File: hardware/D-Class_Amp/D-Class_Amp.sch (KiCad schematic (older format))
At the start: 25 parts, among them J101 Barrel_Jack_MountingPin, J102 AudioJack2, U101 NCP1117-12_TO252, U102 MCP1799T-5002H_TT

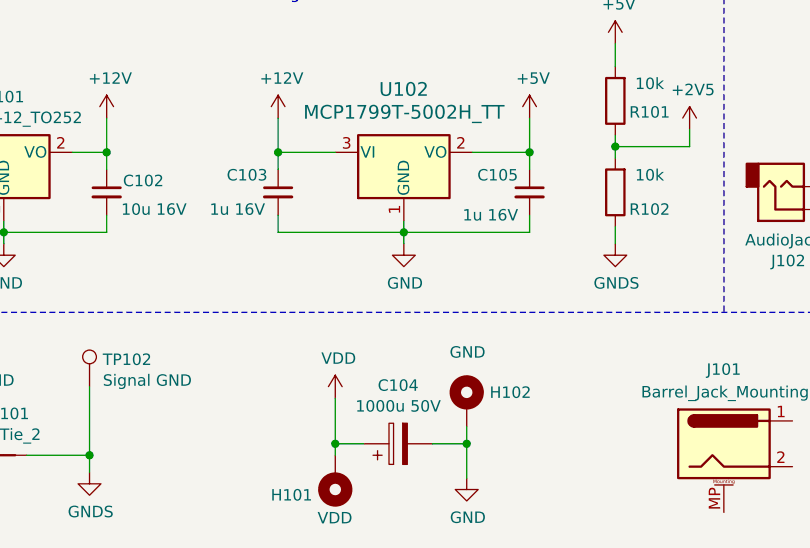
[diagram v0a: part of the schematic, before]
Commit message: Designed the triangle generator PCB layout, and the power switching stage layout
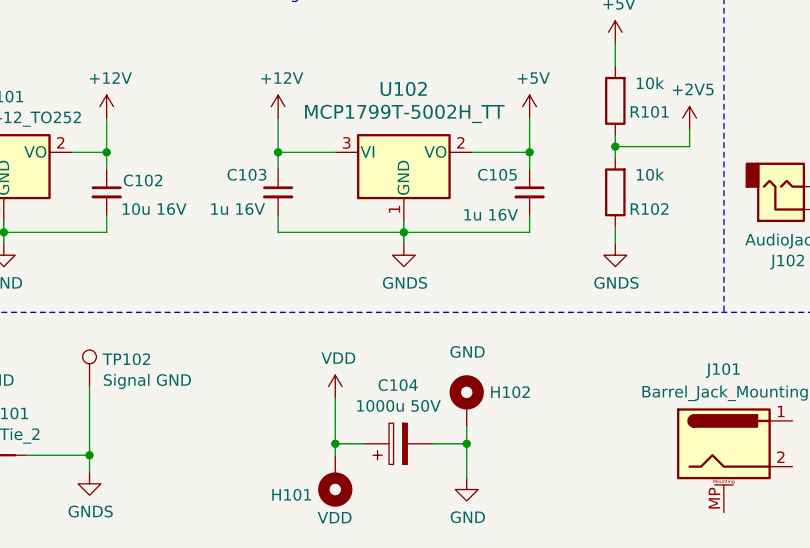
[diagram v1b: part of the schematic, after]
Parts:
- H101, H102: footprint (none) -> MountingHole:MountingHole_3mm_Pad_Via
- NT101: footprint (none) -> NetTie:NetTie-2_SMD_Pad2.0mm
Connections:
- net GND: no longer C103.2, C105.2, U102.1 (GND)
- net GNDS: now also C103.2, C105.2, U102.1 (GND)
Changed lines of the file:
@@
 $EndComp
 $Comp
-L power:GND #PWR0101
+L power:GND #PWR0102
 U 1 1 612A56C1
 P 900 2675
-F 0 "#PWR0101" H 900 2425 50  0001 C CNN
+F 0 "#PWR0102" H 900 2425 50  0001 C CNN
 F 1 "GND" H 905 2502 50  0000 C CNN
 F 2 "" H 900 2675 50  0001 C CNN
@@
 F 0 "NT101" H 1300 2781 50  0000 C CNN
 F 1 "Net-Tie_2" H 1300 2690 50  0000 C CNN
-F 2 "" H 1300 2600 50  0001 C CNN
+F 2 "NetTie:NetTie-2_SMD_Pad2.0mm" H 1300 2600 50  0001 C CNN
 F 3 "~" H 1300 2600 50  0001 C CNN
 	1    1300 2600
@@
 Wire Wire Line
 	1675 2600 1675 2675
-$Comp
-L Connector:TestPoint TP103
-U 1 1 61126C37
-P 5175 800
-F 0 "TP103" H 5233 918 50  0000 L CNN
-F 1 "Audio In" H 5233 827 50  0000 L CNN
-F 2 "TestPoint:TestPoint_THTPad_D2.0mm_Drill1.0mm" H 5375 800 50  0001 C CNN
-F 3 "~" H 5375 800 50  0001 C CNN
-	1    5175 800
-	1    0    0    -1
-$EndComp
-$Comp
-L Connector:TestPoint TP104
-U 1 1 6112780B
-P 6425 800
-F 0 "TP104" H 6483 918 50  0000 L CNN
-F 1 "Input Filter" H 6483 827 50  0000 L CNN
-F 2 "TestPoint:TestPoint_THTPad_D2.0mm_Drill1.0mm" H 6625 800 50  0001 C CNN
-F 3 "~" H 6625 800 50  0001 C CNN
-	1    6425 800
-	1    0    0    -1
-$EndComp
 Wire Wire Line
 	10075 1525 10325 1525
@@
 	1    0    0    -1
 $EndComp
-$Comp
-L Connector:TestPoint TP106
-U 1 1 61129DBB
-P 7775 775
-F 0 "TP106" H 7833 899 50  0000 L CNN
-F 1 "~S-PWM" H 7833 801 50  0000 L CNN
-F 2 "TestPoint:TestPoint_THTPad_D2.0mm_Drill1.0mm" H 7975 775 50  0001 C CNN
-F 3 "~" H 7975 775 50  0001 C CNN
-	1    7775 775
-	1    0    0    -1
-$EndComp
-$Comp
-L Connector:TestPoint TP107
-U 1 1 6112D71A
-P 8825 775
-F 0 "TP107" H 8750 875 50  0000 R CNN
-F 1 "P_Out" H 8550 800 50  0000 L CNN
-F 2 "TestPoint:TestPoint_THTPad_D2.0mm_Drill1.0mm" H 9025 775 50  0001 C CNN
-F 3 "~" H 9025 775 50  0001 C CNN
-	1    8825 775
-	1    0    0    -1
-$EndComp
-$Comp
-L Connector:TestPoint TP108
-U 1 1 6112D764
-P 8975 775
-F 0 "TP108" H 9033 899 50  0000 L CNN
-F 1 "~P_Out" H 9033 801 50  0000 L CNN
-F 2 "TestPoint:TestPoint_THTPad_D2.0mm_Drill1.0mm" H 9175 775 50  0001 C CNN
-F 3 "~" H 9175 775 50  0001 C CNN
-	1    8975 775
-	1    0    0    -1
-$EndComp
 Wire Wire Line
 	8825 775  8825 1325
@@
 Wire Wire Line
 	5175 1425 5375 1425
-$Comp
-L Connector:TestPoint TP110
-U 1 1 6113731F
-P 10325 775
-F 0 "TP110" H 10383 893 50  0000 L CNN
-F 1 "~Speaker_Out" H 10383 802 50  0000 L CNN
-F 2 "TestPoint:TestPoint_THTPad_D2.0mm_Drill1.0mm" H 10525 775 50  0001 C CNN
-F 3 "~" H 10525 775 50  0001 C CNN
-	1    10325 775
-	1    0    0    -1
-$EndComp
 Wire Wire Line
 	10175 775  10175 1325
@@
 Wire Wire Line
 	10325 1525 10425 1525
-$Comp
-L Connector:TestPoint TP105
-U 1 1 6112B1A8
-P 7625 775
-F 0 "TP105" H 7550 875 50  0000 R CNN
-F 1 "S-PWM" H 7300 800 50  0000 L CNN
-F 2 "TestPoint:TestPoint_THTPad_D2.0mm_Drill1.0mm" H 7825 775 50  0001 C CNN
-F 3 "~" H 7825 775 50  0001 C CNN
-	1    7625 775
-	1    0    0    -1
-$EndComp
-$Comp
-L Connector:TestPoint TP109
-U 1 1 611372D5
-P 10175 775
-F 0 "TP109" H 10100 875 50  0000 R CNN
-F 1 "Speaker_Out" H 9700 800 50  0000 L CNN
-F 2 "TestPoint:TestPoint_THTPad_D2.0mm_Drill1.0mm" H 10375 775 50  0001 C CNN
-F 3 "~" H 10375 775 50  0001 C CNN
-	1    10175 775
-	1    0    0    -1
-$EndComp
 Text Notes 850  700  0    50   ~ 0
 12V Reg\n\n
@@
 P 850 1125
 AR Path="/610497A4/611CA11C" Ref="#PWR?"  Part="1"
-AR Path="/611CA11C" Ref="#PWR0102"  Part="1"
-F 0 "#PWR0102" H 850 975 50  0001 C CNN
+AR Path="/611CA11C" Ref="#PWR0101"  Part="1"
+F 0 "#PWR0101" H 850 975 50  0001 C CNN
 F 1 "VDD" H 865 1298 50  0000 C CNN
 F 2 "" H 850 1125 50  0001 C CNN
 F 3 "" H 850 1125 50  0001 C CNN
 	1    850  1125
-	1    0    0    -1
-$EndComp
-$Comp
-L power:GND #PWR?
-U 1 1 611CA122
-P 1300 1675
-AR Path="/610497A4/611CA122" Ref="#PWR?"  Part="1"
-AR Path="/611CA122" Ref="#PWR0103"  Part="1"
-F 0 "#PWR0103" H 1300 1425 50  0001 C CNN
-F 1 "GND" H 1305 1502 50  0000 C CNN
-F 2 "" H 1300 1675 50  0001 C CNN
-F 3 "" H 1300 1675 50  0001 C CNN
-	1    1300 1675
 	1    0    0    -1
 $EndComp
@@
 Text Notes 2350 700  0    50   ~ 0
 5V Reg\n\n
-$Comp
-L power:GND #PWR?
-U 1 1 611FCDB4
-P 3050 1675
-AR Path="/610497A4/611FCDB4" Ref="#PWR?"  Part="1"
-AR Path="/611FCDB4" Ref="#PWR0108"  Part="1"
-F 0 "#PWR0108" H 3050 1425 50  0001 C CNN
-F 1 "GND" H 3055 1502 50  0000 C CNN
-F 2 "" H 3050 1675 50  0001 C CNN
-F 3 "" H 3050 1675 50  0001 C CNN
-	1    3050 1675
-	1    0    0    -1
-$EndComp
 Wire Wire Line
 	3050 1625 3050 1675
 Wire Notes Line
 	450  1975 11225 1975
-$Comp
-L Connector:TestPoint TP101
-U 1 1 6113B2E7
-P 900 2300
-F 0 "TP101" H 958 2418 50  0000 L CNN
-F 1 "Power GND" H 958 2327 50  0000 L CNN
-F 2 "TestPoint:TestPoint_THTPad_D2.0mm_Drill1.0mm" H 1100 2300 50  0001 C CNN
-F 3 "~" H 1100 2300 50  0001 C CNN
-	1    900  2300
-	1    0    0    -1
-$EndComp
-$Comp
-L Connector:TestPoint TP102
-U 1 1 6113B863
-P 1675 2300
-F 0 "TP102" H 1733 2418 50  0000 L CNN
-F 1 "Signal GND" H 1733 2327 50  0000 L CNN
-F 2 "TestPoint:TestPoint_THTPad_D2.0mm_Drill1.0mm" H 1875 2300 50  0001 C CNN
-F 3 "~" H 1875 2300 50  0001 C CNN
-	1    1675 2300
-	1    0    0    -1
-$EndComp
 Wire Wire Line
 	900  2300 900  2600
@@
 F 0 "H102" H 3425 2424 50  0000 L CNN
 F 1 "GND" H 3250 2600 50  0000 L CNN
-F 2 "" H 3325 2375 50  0001 C CNN
+F 2 "MountingHole:MountingHole_3mm_Pad_Via" H 3325 2375 50  0001 C CNN
 F 3 "~" H 3325 2375 50  0001 C CNN
 	1    3325 2375
@@
 F 0 "H101" H 2850 2775 50  0000 L CNN
 F 1 "VDD" H 2675 2875 50  0000 L CNN
-F 2 "" H 2750 2700 50  0001 C CNN
+F 2 "MountingHole:MountingHole_3mm_Pad_Via" H 2750 2700 50  0001 C CNN
 F 3 "~" H 2750 2700 50  0001 C CNN
 	1    2750 2700
@@
 	1    0    0    -1
 $EndComp
+$Comp
+L Connector:TestPoint TP110
+U 1 1 6113731F
+P 10325 775
+F 0 "TP110" H 10383 893 50  0000 L CNN
+F 1 "~Speaker_Out" H 10383 802 50  0000 L CNN
+F 2 "TestPoint:TestPoint_THTPad_D2.0mm_Drill1.0mm" H 10525 775 50  0001 C CNN
+F 3 "~" H 10525 775 50  0001 C CNN
+	1    10325 775
+	1    0    0    -1
+$EndComp
+$Comp
+L Connector:TestPoint TP109
+U 1 1 611372D5
+P 10175 775
+F 0 "TP109" H 10100 875 50  0000 R CNN
+F 1 "Speaker_Out" H 9700 800 50  0000 L CNN
+F 2 "TestPoint:TestPoint_THTPad_D2.0mm_Drill1.0mm" H 10375 775 50  0001 C CNN
+F 3 "~" H 10375 775 50  0001 C CNN
+	1    10175 775
+	1    0    0    -1
+$EndComp
+$Comp
+L Connector:TestPoint TP108
+U 1 1 6112D764
+P 8975 775
+F 0 "TP108" H 9033 899 50  0000 L CNN
+F 1 "~P_Out" H 9033 801 50  0000 L CNN
+F 2 "TestPoint:TestPoint_THTPad_D2.0mm_Drill1.0mm" H 9175 775 50  0001 C CNN
+F 3 "~" H 9175 775 50  0001 C CNN
+	1    8975 775
+	1    0    0    -1
+$EndComp
+$Comp
+L Connector:TestPoint TP107
+U 1 1 6112D71A
+P 8825 775
+F 0 "TP107" H 8750 875 50  0000 R CNN
+F 1 "P_Out" H 8550 800 50  0000 L CNN
+F 2 "TestPoint:TestPoint_THTPad_D2.0mm_Drill1.0mm" H 9025 775 50  0001 C CNN
+F 3 "~" H 9025 775 50  0001 C CNN
+	1    8825 775
+	1    0    0    -1
+$EndComp
+$Comp
+L Connector:TestPoint TP106
+U 1 1 61129DBB
+P 7775 775
+F 0 "TP106" H 7833 899 50  0000 L CNN
+F 1 "~S-PWM" H 7833 801 50  0000 L CNN
+F 2 "TestPoint:TestPoint_THTPad_D2.0mm_Drill1.0mm" H 7975 775 50  0001 C CNN
+F 3 "~" H 7975 775 50  0001 C CNN
+	1    7775 775
+	1    0    0    -1
+$EndComp
+$Comp
+L Connector:TestPoint TP105
+U 1 1 6112B1A8
+P 7625 775
+F 0 "TP105" H 7550 875 50  0000 R CNN
+F 1 "S-PWM" H 7300 800 50  0000 L CNN
+F 2 "TestPoint:TestPoint_THTPad_D2.0mm_Drill1.0mm" H 7825 775 50  0001 C CNN
+F 3 "~" H 7825 775 50  0001 C CNN
+	1    7625 775
+	1    0    0    -1
+$EndComp
+$Comp
+L Connector:TestPoint TP104
+U 1 1 6112780B
+P 6425 800
+F 0 "TP104" H 6483 918 50  0000 L CNN
+F 1 "Input Filter" H 6483 827 50  0000 L CNN
+F 2 "TestPoint:TestPoint_THTPad_D2.0mm_Drill1.0mm" H 6625 800 50  0001 C CNN
+F 3 "~" H 6625 800 50  0001 C CNN
+	1    6425 800
+	1    0    0    -1
+$EndComp
+$Comp
+L Connector:TestPoint TP103
+U 1 1 61126C37
+P 5175 800
+F 0 "TP103" H 5233 918 50  0000 L CNN
+F 1 "Audio In" H 5233 827 50  0000 L CNN
+F 2 "TestPoint:TestPoint_THTPad_D2.0mm_Drill1.0mm" H 5375 800 50  0001 C CNN
+F 3 "~" H 5375 800 50  0001 C CNN
+	1    5175 800
+	1    0    0    -1
+$EndComp
+$Comp
+L Connector:TestPoint TP102
+U 1 1 6113B863
+P 1675 2300
+F 0 "TP102" H 1733 2418 50  0000 L CNN
+F 1 "Signal GND" H 1733 2327 50  0000 L CNN
+F 2 "TestPoint:TestPoint_THTPad_D2.0mm_Drill1.0mm" H 1875 2300 50  0001 C CNN
+F 3 "~" H 1875 2300 50  0001 C CNN
+	1    1675 2300
+	1    0    0    -1
+$EndComp
+$Comp
+L Connector:TestPoint TP101
+U 1 1 6113B2E7
+P 900 2300
+F 0 "TP101" H 958 2418 50  0000 L CNN
+F 1 "Power GND" H 958 2327 50  0000 L CNN
+F 2 "TestPoint:TestPoint_THTPad_D2.0mm_Drill1.0mm" H 1100 2300 50  0001 C CNN
+F 3 "~" H 1100 2300 50  0001 C CNN
+	1    900  2300
+	1    0    0    -1
+$EndComp
+$Comp
+L power:GNDS #PWR0103
+U 1 1 61218DB5
+P 3050 1675
+F 0 "#PWR0103" H 3050 1425 50  0001 C CNN
+F 1 "GNDS" H 3055 1502 50  0000 C CNN
+F 2 "" H 3050 1675 50  0001 C CNN
+F 3 "" H 3050 1675 50  0001 C CNN
+	1    3050 1675
+	1    0    0    -1
+$EndComp
+$Comp
+L power:GND #PWR?
+U 1 1 611FCDB4
+P 1300 1675
+AR Path="/610497A4/611FCDB4" Ref="#PWR?"  Part="1"
+AR Path="/611FCDB4" Ref="#PWR0108"  Part="1"
+F 0 "#PWR0108" H 1300 1425 50  0001 C CNN
+F 1 "GND" H 1305 1502 50  0000 C CNN
+F 2 "" H 1300 1675 50  0001 C CNN
+F 3 "" H 1300 1675 50  0001 C CNN
+	1    1300 1675
+	1    0    0    -1
+$EndComp

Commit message: placed and routed all components, fixed the MOSFET footprints, and added all 3D models.
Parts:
- LS101: footprint (none) -> Speaker:Speaker
- TP101, TP102, TP103, TP104, TP105, TP106, TP107, TP108, TP109, TP110: footprint TestPoint:TestPoint_THTPad_D2.0mm_Drill1.0mm -> TestPoint:TestPoint_THTPad_D1.0mm_Drill0.5mm
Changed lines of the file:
@@
 F 0 "LS101" H 10895 1371 50  0000 L CNN
 F 1 "Speaker" H 10895 1280 50  0000 L CNN
-F 2 "" H 10725 1175 50  0001 C CNN
+F 2 "Speaker:Speaker" H 10725 1175 50  0001 C CNN
 F 3 "~" H 10715 1325 50  0001 C CNN
 	1    10725 1375
@@
 F 0 "TP110" H 10383 893 50  0000 L CNN
 F 1 "~Speaker_Out" H 10383 802 50  0000 L CNN
-F 2 "TestPoint:TestPoint_THTPad_D2.0mm_Drill1.0mm" H 10525 775 50  0001 C CNN
+F 2 "TestPoint:TestPoint_THTPad_D1.0mm_Drill0.5mm" H 10525 775 50  0001 C CNN
 F 3 "~" H 10525 775 50  0001 C CNN
 	1    10325 775
@@
 F 0 "TP109" H 10100 875 50  0000 R CNN
 F 1 "Speaker_Out" H 9700 800 50  0000 L CNN
-F 2 "TestPoint:TestPoint_THTPad_D2.0mm_Drill1.0mm" H 10375 775 50  0001 C CNN
+F 2 "TestPoint:TestPoint_THTPad_D1.0mm_Drill0.5mm" H 10375 775 50  0001 C CNN
 F 3 "~" H 10375 775 50  0001 C CNN
 	1    10175 775
@@
 F 0 "TP108" H 9033 899 50  0000 L CNN
 F 1 "~P_Out" H 9033 801 50  0000 L CNN
-F 2 "TestPoint:TestPoint_THTPad_D2.0mm_Drill1.0mm" H 9175 775 50  0001 C CNN
+F 2 "TestPoint:TestPoint_THTPad_D1.0mm_Drill0.5mm" H 9175 775 50  0001 C CNN
 F 3 "~" H 9175 775 50  0001 C CNN
 	1    8975 775
@@
 F 0 "TP107" H 8750 875 50  0000 R CNN
 F 1 "P_Out" H 8550 800 50  0000 L CNN
-F 2 "TestPoint:TestPoint_THTPad_D2.0mm_Drill1.0mm" H 9025 775 50  0001 C CNN
+F 2 "TestPoint:TestPoint_THTPad_D1.0mm_Drill0.5mm" H 9025 775 50  0001 C CNN
 F 3 "~" H 9025 775 50  0001 C CNN
 	1    8825 775
@@
 F 0 "TP106" H 7833 899 50  0000 L CNN
 F 1 "~S-PWM" H 7833 801 50  0000 L CNN
-F 2 "TestPoint:TestPoint_THTPad_D2.0mm_Drill1.0mm" H 7975 775 50  0001 C CNN
+F 2 "TestPoint:TestPoint_THTPad_D1.0mm_Drill0.5mm" H 7975 775 50  0001 C CNN
 F 3 "~" H 7975 775 50  0001 C CNN
 	1    7775 775
@@
 F 0 "TP105" H 7550 875 50  0000 R CNN
 F 1 "S-PWM" H 7300 800 50  0000 L CNN
-F 2 "TestPoint:TestPoint_THTPad_D2.0mm_Drill1.0mm" H 7825 775 50  0001 C CNN
+F 2 "TestPoint:TestPoint_THTPad_D1.0mm_Drill0.5mm" H 7825 775 50  0001 C CNN
 F 3 "~" H 7825 775 50  0001 C CNN
 	1    7625 775
@@
 F 0 "TP104" H 6483 918 50  0000 L CNN
 F 1 "Input Filter" H 6483 827 50  0000 L CNN
-F 2 "TestPoint:TestPoint_THTPad_D2.0mm_Drill1.0mm" H 6625 800 50  0001 C CNN
+F 2 "TestPoint:TestPoint_THTPad_D1.0mm_Drill0.5mm" H 6625 800 50  0001 C CNN
 F 3 "~" H 6625 800 50  0001 C CNN
 	1    6425 800
@@
 F 0 "TP103" H 5233 918 50  0000 L CNN
 F 1 "Audio In" H 5233 827 50  0000 L CNN
-F 2 "TestPoint:TestPoint_THTPad_D2.0mm_Drill1.0mm" H 5375 800 50  0001 C CNN
+F 2 "TestPoint:TestPoint_THTPad_D1.0mm_Drill0.5mm" H 5375 800 50  0001 C CNN
 F 3 "~" H 5375 800 50  0001 C CNN
 	1    5175 800
@@
 F 0 "TP102" H 1733 2418 50  0000 L CNN
 F 1 "Signal GND" H 1733 2327 50  0000 L CNN
-F 2 "TestPoint:TestPoint_THTPad_D2.0mm_Drill1.0mm" H 1875 2300 50  0001 C CNN
+F 2 "TestPoint:TestPoint_THTPad_D1.0mm_Drill0.5mm" H 1875 2300 50  0001 C CNN
 F 3 "~" H 1875 2300 50  0001 C CNN
 	1    1675 2300
@@
 F 0 "TP101" H 958 2418 50  0000 L CNN
 F 1 "Power GND" H 958 2327 50  0000 L CNN
-F 2 "TestPoint:TestPoint_THTPad_D2.0mm_Drill1.0mm" H 1100 2300 50  0001 C CNN
+F 2 "TestPoint:TestPoint_THTPad_D1.0mm_Drill0.5mm" H 1100 2300 50  0001 C CNN
 F 3 "~" H 1100 2300 50  0001 C CNN
 	1    900  2300

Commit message: UwU
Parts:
- added H103: SIG, MountingHole:MountingHole_3mm_Pad_Via, symbol Mechanical:MountingHole_Pad
- added H104: GNDS, MountingHole:MountingHole_3mm_Pad_Via, symbol Mechanical:MountingHole_Pad
- added H105, H106, H107, H108: MountingHole_Pad, MountingHole:MountingHole_3.2mm_M3_ISO14580_Pad, symbol Mechanical:MountingHole_Pad
- J101: value Barrel_Jack_MountingPin -> P_IN; footprint (none) -> Connector_BarrelJack:BarrelJack_Horizontal; DigiKey Price (none) -> 1.20; Part Number (none) -> PJ-002BH
- J102: footprint Connector_Audio:Jack_3.5mm_CUI_SJ-3523-SMT_Horizontal -> CUI_MJ-63022A:CUI_MJ-63022A
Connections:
- net GND: now also J101.2, H105.1, H106.1, H107.1, H108.1
- net GNDS: now also H104.1
- net Input_Stage/SIG_IN: now also H103.1
- net VDD: now also J101.1
- no-connect marks 0 -> 1
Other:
- moved on the sheet: TP103, TP104
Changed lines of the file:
@@
 $EndDescr
 $Sheet
-S 5375 1125 850  600
+S 5475 1125 850  600
 U 6104907A
 F0 "Input_Stage" 50
 F1 "Input_Stage.sch" 50
-F2 "SIG_IN" I L 5375 1425 50
-F3 "FILT_OUT" O R 6225 1425 50
+F2 "SIG_IN" I L 5475 1425 50
+F3 "FILT_OUT" O R 6325 1425 50
 $EndSheet
 $Sheet
@@
 $EndSheet
 Wire Wire Line
-	6225 1425 6425 1425
-Wire Wire Line
 	10425 1325 10425 1375
 Wire Wire Line
@@
 F 0 "J102" H 4732 1750 50  0000 C CNN
 F 1 "AudioJack2" H 4732 1659 50  0000 C CNN
-F 2 "Connector_Audio:Jack_3.5mm_CUI_SJ-3523-SMT_Horizontal" H 4700 1425 50  0001 C CNN
+F 2 "CUI_MJ-63022A:CUI_MJ-63022A" H 4700 1425 50  0001 C CNN
 F 3 "~" H 4700 1425 50  0001 C CNN
 	1    4700 1425
 	1    0    0    1
 $EndComp
-Wire Wire Line
-	4900 1425 5175 1425
 $Comp
 L power:GNDS #PWR0114
@@
 	7775 1525 7875 1525
 Wire Wire Line
-	6425 800  6425 1425
-Connection ~ 6425 1425
-Wire Wire Line
-	6425 1425 6625 1425
-Wire Wire Line
-	5175 800  5175 1425
-Connection ~ 5175 1425
-Wire Wire Line
-	5175 1425 5375 1425
+	6475 800  6475 1425
+Wire Wire Line
+	5375 800  5375 950
 Wire Wire Line
 	10175 775  10175 1325
@@
 U 1 1 612622C7
 P 4450 2550
-F 0 "J101" H 4450 2875 50  0000 C CNN
-F 1 "Barrel_Jack_MountingPin" H 4507 2776 50  0000 C CNN
-F 2 "" H 4500 2510 50  0001 C CNN
+F 0 "J101" H 4450 2850 50  0000 C CNN
+F 1 "P_IN" H 4450 2750 50  0000 C CNN
+F 2 "Connector_BarrelJack:BarrelJack_Horizontal" H 4500 2510 50  0001 C CNN
 F 3 "~" H 4500 2510 50  0001 C CNN
+F 4 "1.20" H 4450 2550 50  0001 C CNN "DigiKey Price"
+F 5 "PJ-002BH" H 4450 2550 50  0001 C CNN "Part Number"
 	1    4450 2550
 	1    0    0    -1
@@
 L Connector:TestPoint TP104
 U 1 1 6112780B
-P 6425 800
-F 0 "TP104" H 6483 918 50  0000 L CNN
-F 1 "Input Filter" H 6483 827 50  0000 L CNN
-F 2 "TestPoint:TestPoint_THTPad_D1.0mm_Drill0.5mm" H 6625 800 50  0001 C CNN
-F 3 "~" H 6625 800 50  0001 C CNN
-	1    6425 800
+P 6475 800
+F 0 "TP104" H 6533 918 50  0000 L CNN
+F 1 "Input Filter" H 6533 827 50  0000 L CNN
+F 2 "TestPoint:TestPoint_THTPad_D1.0mm_Drill0.5mm" H 6675 800 50  0001 C CNN
+F 3 "~" H 6675 800 50  0001 C CNN
+	1    6475 800
 	1    0    0    -1
 $EndComp
@@
 L Connector:TestPoint TP103
 U 1 1 61126C37
-P 5175 800
-F 0 "TP103" H 5233 918 50  0000 L CNN
-F 1 "Audio In" H 5233 827 50  0000 L CNN
-F 2 "TestPoint:TestPoint_THTPad_D1.0mm_Drill0.5mm" H 5375 800 50  0001 C CNN
-F 3 "~" H 5375 800 50  0001 C CNN
-	1    5175 800
+P 5375 800
+F 0 "TP103" H 5433 918 50  0000 L CNN
+F 1 "Audio In" H 5433 827 50  0000 L CNN
+F 2 "TestPoint:TestPoint_THTPad_D1.0mm_Drill0.5mm" H 5575 800 50  0001 C CNN
+F 3 "~" H 5575 800 50  0001 C CNN
+	1    5375 800
 	1    0    0    -1
 $EndComp
@@
 	1    0    0    -1
 $EndComp
+$Comp
+L Mechanical:MountingHole_Pad H103
+U 1 1 61192847
+P 5050 800
+F 0 "H103" H 5150 849 50  0000 L CNN
+F 1 "SIG" H 4975 975 50  0000 L CNN
+F 2 "MountingHole:MountingHole_3mm_Pad_Via" H 5050 800 50  0001 C CNN
+F 3 "~" H 5050 800 50  0001 C CNN
+	1    5050 800
+	1    0    0    -1
+$EndComp
+Wire Wire Line
+	6325 1425 6475 1425
+Connection ~ 6475 1425
+Wire Wire Line
+	6475 1425 6625 1425
+Connection ~ 5375 1425
+Wire Wire Line
+	5375 1425 5475 1425
+Wire Wire Line
+	4900 1425 5375 1425
+Wire Wire Line
+	5050 1525 5050 1375
+Connection ~ 5050 1525
+Wire Wire Line
+	5050 900  5050 950
+Wire Wire Line
+	5050 950  5375 950
+Connection ~ 5375 950
+Wire Wire Line
+	5375 950  5375 1425
+$Comp
+L Mechanical:MountingHole_Pad H104
+U 1 1 61173615
+P 5050 1275
+F 0 "H104" H 5150 1324 50  0000 L CNN
+F 1 "GNDS" H 5050 1450 50  0000 C CNN
+F 2 "MountingHole:MountingHole_3mm_Pad_Via" H 5050 1275 50  0001 C CNN
+F 3 "~" H 5050 1275 50  0001 C CNN
+	1    5050 1275
+	1    0    0    -1
+$EndComp
+NoConn ~ 4450 2850
+$Comp
+L power:VDD #PWR?
+U 1 1 611BD52F
+P 4800 2400
+AR Path="/610497A4/611BD52F" Ref="#PWR?"  Part="1"
+AR Path="/611BD52F" Ref="#PWR0115"  Part="1"
+F 0 "#PWR0115" H 4800 2250 50  0001 C CNN
+F 1 "VDD" H 4815 2573 50  0000 C CNN
+F 2 "" H 4800 2400 50  0001 C CNN
+F 3 "" H 4800 2400 50  0001 C CNN
+	1    4800 2400
+	1    0    0    -1
+$EndComp
+$Comp
+L power:GND #PWR0116
+U 1 1 611C0B92
+P 4800 2700
+F 0 "#PWR0116" H 4800 2450 50  0001 C CNN
+F 1 "GND" H 4805 2527 50  0000 C CNN
+F 2 "" H 4800 2700 50  0001 C CNN
+F 3 "" H 4800 2700 50  0001 C CNN
+	1    4800 2700
+	1    0    0    -1
+$EndComp
+Wire Wire Line
+	4750 2650 4800 2650
+Wire Wire Line
+	4800 2650 4800 2700
+Wire Wire Line
+	4750 2450 4800 2450
+Wire Wire Line
+	4800 2450 4800 2400
+$Comp
+L Mechanical:MountingHole_Pad H105
+U 1 1 611E3235
+P 6600 2600
+F 0 "H105" H 6700 2649 50  0000 L CNN
+F 1 "MountingHole_Pad" H 6700 2558 50  0000 L CNN
+F 2 "MountingHole:MountingHole_3.2mm_M3_ISO14580_Pad" H 6600 2600 50  0001 C CNN
+F 3 "~" H 6600 2600 50  0001 C CNN
+	1    6600 2600
+	1    0    0    -1
+$EndComp
+$Comp
+L Mechanical:MountingHole_Pad H106
+U 1 1 611E3AD1
+P 6600 3200
+F 0 "H106" H 6700 3249 50  0000 L CNN
+F 1 "MountingHole_Pad" H 6700 3158 50  0000 L CNN
+F 2 "MountingHole:MountingHole_3.2mm_M3_ISO14580_Pad" H 6600 3200 50  0001 C CNN
+F 3 "~" H 6600 3200 50  0001 C CNN
+	1    6600 3200
+	1    0    0    -1
+$EndComp
+$Comp
+L Mechanical:MountingHole_Pad H107
+U 1 1 611E3C5C
+P 7750 2600
+F 0 "H107" H 7850 2649 50  0000 L CNN
+F 1 "MountingHole_Pad" H 7850 2558 50  0000 L CNN
+F 2 "MountingHole:MountingHole_3.2mm_M3_ISO14580_Pad" H 7750 2600 50  0001 C CNN
+F 3 "~" H 7750 2600 50  0001 C CNN
+	1    7750 2600
+	1    0    0    -1
+$EndComp
+$Comp
+L Mechanical:MountingHole_Pad H108
+U 1 1 611E3E0A
+P 7750 3200
+F 0 "H108" H 7850 3249 50  0000 L CNN
+F 1 "MountingHole_Pad" H 7850 3158 50  0000 L CNN
+F 2 "MountingHole:MountingHole_3.2mm_M3_ISO14580_Pad" H 7750 3200 50  0001 C CNN
+F 3 "~" H 7750 3200 50  0001 C CNN
+	1    7750 3200
+	1    0    0    -1
+$EndComp
+$Comp
+L power:GND #PWR0118
+U 1 1 611E8313
+P 6600 3300
+F 0 "#PWR0118" H 6600 3050 50  0001 C CNN
+F 1 "GND" H 6605 3127 50  0000 C CNN
+F 2 "" H 6600 3300 50  0001 C CNN
+F 3 "" H 6600 3300 50  0001 C CNN
+	1    6600 3300
+	1    0    0    -1
+$EndComp
+$Comp
+L power:GND #PWR0117
+U 1 1 611E894E
+P 6600 2700
+F 0 "#PWR0117" H 6600 2450 50  0001 C CNN
+F 1 "GND" H 6605 2527 50  0000 C CNN
+F 2 "" H 6600 2700 50  0001 C CNN
+F 3 "" H 6600 2700 50  0001 C CNN
+	1    6600 2700
+	1    0    0    -1
+$EndComp
+$Comp
+L power:GND #PWR0119
+U 1 1 611E8D8E
+P 7750 2700
+F 0 "#PWR0119" H 7750 2450 50  0001 C CNN
+F 1 "GND" H 7755 2527 50  0000 C CNN
+F 2 "" H 7750 2700 50  0001 C CNN
+F 3 "" H 7750 2700 50  0001 C CNN
+	1    7750 2700
+	1    0    0    -1
+$EndComp
+$Comp
+L power:GND #PWR0120
+U 1 1 611E9089
+P 7750 3300
+F 0 "#PWR0120" H 7750 3050 50  0001 C CNN
+F 1 "GND" H 7755 3127 50  0000 C CNN
+F 2 "" H 7750 3300 50  0001 C CNN
+F 3 "" H 7750 3300 50  0001 C CNN
+	1    7750 3300
+	1    0    0    -1
+$EndComp

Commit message: PCB done POG
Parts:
- J102: DigiKey Price (none) -> 2.27; Part Number (none) -> MJ-63022A
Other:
- moved on the sheet: C104, H101, H102, H105, H106, H107, H108, J101, NT101, TP101, TP102
